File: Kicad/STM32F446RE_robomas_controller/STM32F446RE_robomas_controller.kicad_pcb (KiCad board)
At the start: 2 copper layers, 100 x 100 mm, 5 parts, among them U3 NUCLEO-F446RE

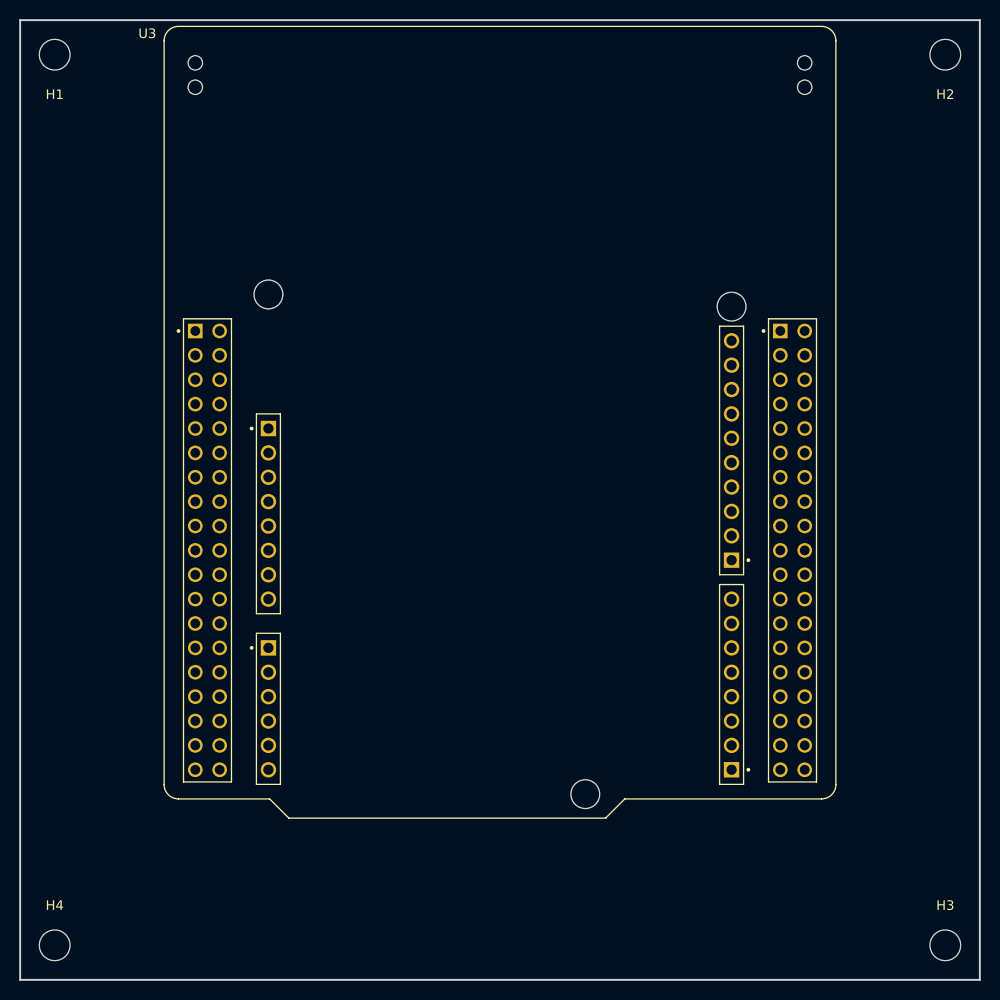
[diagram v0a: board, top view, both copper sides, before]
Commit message: robomas用の回路完成
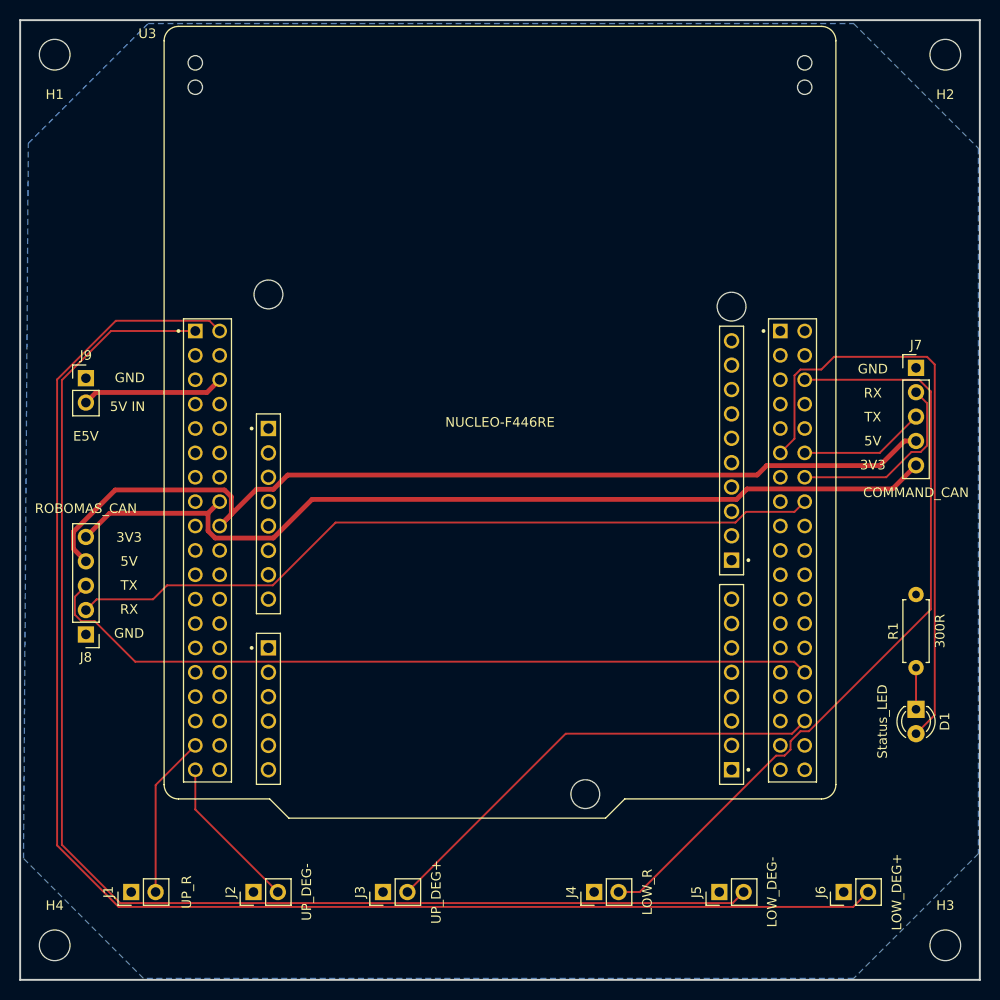
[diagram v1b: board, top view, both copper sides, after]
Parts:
- added D1: Status_LED, LED_THT:LED_D3.0mm, F.Cu at (176.0, 100.0)
- added J1: UP_R, Connector_PinHeader_2.54mm:PinHeader_1x02_P2.54mm_Vertical, F.Cu at (94.2, 119.0)
- added J2: UP_DEG-, Connector_PinHeader_2.54mm:PinHeader_1x02_P2.54mm_Vertical, F.Cu at (107.0, 119.0)
- added J3: UP_DEG+, Connector_PinHeader_2.54mm:PinHeader_1x02_P2.54mm_Vertical, F.Cu at (120.5, 119.0)
- added J4: LOW_R, Connector_PinHeader_2.54mm:PinHeader_1x02_P2.54mm_Vertical, F.Cu at (142.5, 119.0)
- added J5: LOW_DEG-, Connector_PinHeader_2.54mm:PinHeader_1x02_P2.54mm_Vertical, F.Cu at (155.5, 119.0)
- added J6: LOW_DEG+, Connector_PinHeader_2.54mm:PinHeader_1x02_P2.54mm_Vertical, F.Cu at (168.5, 119.0)
- added J7: COMMAND_CAN, Connector_PinHeader_2.54mm:PinHeader_1x05_P2.54mm_Vertical, F.Cu at (176.0, 64.4)
- added J8: ROBOMAS_CAN, Connector_PinHeader_2.54mm:PinHeader_1x05_P2.54mm_Vertical, F.Cu at (89.5, 92.2)
- added J9: E5V, Connector_PinHeader_2.54mm:PinHeader_1x02_P2.54mm_Vertical, F.Cu at (89.5, 65.5)
- added R1: 300R, Resistor_THT:R_Axial_DIN0207_L6.3mm_D2.5mm_P7.62mm_Horizontal, F.Cu at (176.0, 95.6)
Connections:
- U3 pad CN10_11: unconnected-(U3B-PA5-PadCN10_11) -> /Status_LED
- U3 pad CN10_12: unconnected-(U3B-PA12-PadCN10_12) -> /COMMAND_CAN_TX
- U3 pad CN10_14: unconnected-(U3B-PA11-PadCN10_14) -> /COMMAND_CAN_RX
- U3 pad CN10_16: unconnected-(U3B-PB12-PadCN10_16) -> /ROBOMAS_CAN_RX
- U3 pad CN10_20: unconnected-(U3B-CN10_GND__1-PadCN10_20) -> GND
- U3 pad CN10_30: unconnected-(U3B-PB13-PadCN10_30) -> /ROBOMAS_CAN_TX
- U3 pad CN10_32: unconnected-(U3B-AGND-PadCN10_32) -> GND
- U3 pad CN10_34: unconnected-(U3B-PC4-PadCN10_34) -> /UPPER_ARM_DEG_OVER_LIMIT
- U3 pad CN10_6: unconnected-(U3B-PC5-PadCN10_6) -> /LOWER_ARM_R_LIMIT
- U3 pad CN10_9: unconnected-(U3B-CN10_GND-PadCN10_9) -> GND
- U3 pad CN7_1: unconnected-(U3A-PC10-PadCN7_1) -> /LOWER_ARM_DEG_UNDER_LIMIT
- U3 pad CN7_16: unconnected-(U3A-CN7_+3V3-PadCN7_16) -> +3.3V
- U3 pad CN7_18: unconnected-(U3A-CN7_+5V-PadCN7_18) -> +5V
- U3 pad CN7_2: unconnected-(U3A-PC11-PadCN7_2) -> /LOWER_ARM_DEG_OVER_LIMIT
- U3 pad CN7_35: unconnected-(U3A-PC2-PadCN7_35) -> /UPPER_ARM_R_LIMIT
- U3 pad CN7_37: unconnected-(U3A-PC3-PadCN7_37) -> /UPPER_ARM_DEG_UNDER_LIMIT
- U3 pad CN7_6: unconnected-(U3A-E5V-PadCN7_6) -> /E5V
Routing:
- net /LOWER_ARM_DEG_OVER_LIMIT: track 0.00 -> 156.3 mm
- net /LOWER_ARM_DEG_UNDER_LIMIT: track 0.00 -> 138.5 mm
- net +5V: track 0.00 -> 101.9 mm
- net +3.3V: track 0.00 -> 94.5 mm
- net /ROBOMAS_CAN_TX: track 0.00 -> 82.0 mm
- net /LOWER_ARM_R_LIMIT: track 0.00 -> 81.6 mm
- net /ROBOMAS_CAN_RX: track 0.00 -> 79.6 mm
- net /Status_LED: track 0.00 -> 63.7 mm
- net /UPPER_ARM_DEG_OVER_LIMIT: track 0.00 -> 48.8 mm
- net /COMMAND_CAN_RX: track 0.00 -> 20.2 mm
- net /UPPER_ARM_R_LIMIT: track 0.00 -> 17.0 mm
- net /UPPER_ARM_DEG_UNDER_LIMIT: track 0.00 -> 16.3 mm
- net /E5V: track 0.00 -> 14.9 mm
- net /COMMAND_CAN_TX: track 0.00 -> 13.2 mm
- net Net-(D1-K): track 0.00 -> 4.34 mm
- added copper zone on B.Cu, net GND
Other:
- board text added: "3V3"
- board text added: "5V"
- board text added: "5V IN"
- board text added: "GND"
- board text added: "RX"
- board text added: "TX"

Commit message: 回路完成
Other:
- board text added: "Catchrobo_2026 robomas_controller 2026/8/20 K.Oshima"
- board text added: "ピン 用途 設定/信号 PA11 ESP32側 CAN受信 CAN1_RX / COMMAND_CAN_RX PA12 ESP32側 CAN送信 CAN1_TX / COMMAND_CAN_TX PB12 RoboMaster側 CAN受信 CAN2_RX / ROBOMAS_CAN_RX PB13 RoboMaster側 CAN送信 CAN2_TX / ROBOMAS_CAN_TX PC2 上アーム R リミット GPIO Input / Pull-up PC3 上アーム角度 下限 GPIO Input / Pull-up PC4 上アーム角度 上限 GPIO Input / Pull-up PC5 下アーム R リミット GPIO Input / Pull-up PC10 下アーム角度 下限 GPIO Input / Pull-up PC11 下アーム角度 上限 GPIO Input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"
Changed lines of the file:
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@@
+		)
+	)
+	(gr_text "Catchrobo_2026 robomas_controller\n2026/8/20 K.Oshima"
+		(at 160.5 32 0)
+		(layer "B.SilkS")
+		(effects
+			(font
+				(size 1 1)
+				(thickness 0.1)
+			)
+			(justify left bottom mirror)
+		)
+	)
+	(gr_text "ピン			用途					設定/信号\nPA11		ESP32側 CAN受信		CAN1_RX / COMMAND_CAN_RX\nPA12		ESP32側 CAN送信		CAN1_TX / COMMAND_CAN_TX\nPB12		RoboMaster側 CAN受信	CAN2_RX / ROBOMAS_CAN_RX\nPB13		RoboMaster側 CAN送信	CAN2_TX / ROBOMAS_CAN_TX\nPC2			上アーム R リミット			GPIO Input / Pull-up\nPC3			上アーム角度 下限			GPIO Input / Pull-up\nPC4			上アーム角度 上限			GPIO Input / Pull-up\nPC5			下アーム R リミット			GPIO Input / Pull-up\nPC10		下アーム角度 下限			GPIO Input / Pull-up\nPC11		下アーム角度 上限			GPIO Input / Pull-up\nPA5			動作確認LED			GPIO Output / Status_LED"
+		(at 142 48.5 90)
+		(layer "B.SilkS")
+		(effects
+			(font
+				(size 1 1)
+				(thickness 0.1)
+			)
+			(justify left bottom mirror)
 		)
 	)
